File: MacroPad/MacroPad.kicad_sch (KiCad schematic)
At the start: 1 part

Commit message: RGB LED Circuit
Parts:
- added D? (x12): WS2812B, LED_SMD:LED_WS2812B_PLCC4_5.0x5.0mm_P3.2mm, symbol LED:WS2812B
- added R?: 470R, symbol Device:R
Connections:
- net GND: now reaches U?.14 (GND)
- net GND: now also D?.3 (VSS), D?.3 (VSS), D?.3 (VSS), D?.3 (VSS), D?.3 (VSS), D?.3 (VSS), D?.3 (VSS), D?.3 (VSS), D?.3 (VSS), D?.3 (VSS), D?.3 (VSS), D?.3 (VSS)
- net Vin: now reaches U?.19 (5V)
- net Vin: now also D?.1 (VDD), D?.1 (VDD), D?.1 (VDD), D?.1 (VDD), D?.1 (VDD), D?.1 (VDD), D?.1 (VDD), D?.1 (VDD), D?.1 (VDD), D?.1 (VDD), D?.1 (VDD), D?.1 (VDD)
- net DATA: now reaches U?.33 (GPIO21)
- net DATA: now also R?.1
- new net: D?.2 (DOUT), D?.4 (DIN) (x11)
- new net: D?.4 (DIN), R?.2
- no-connect marks 0 -> 1
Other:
- note added: "RGB LED Circuit"

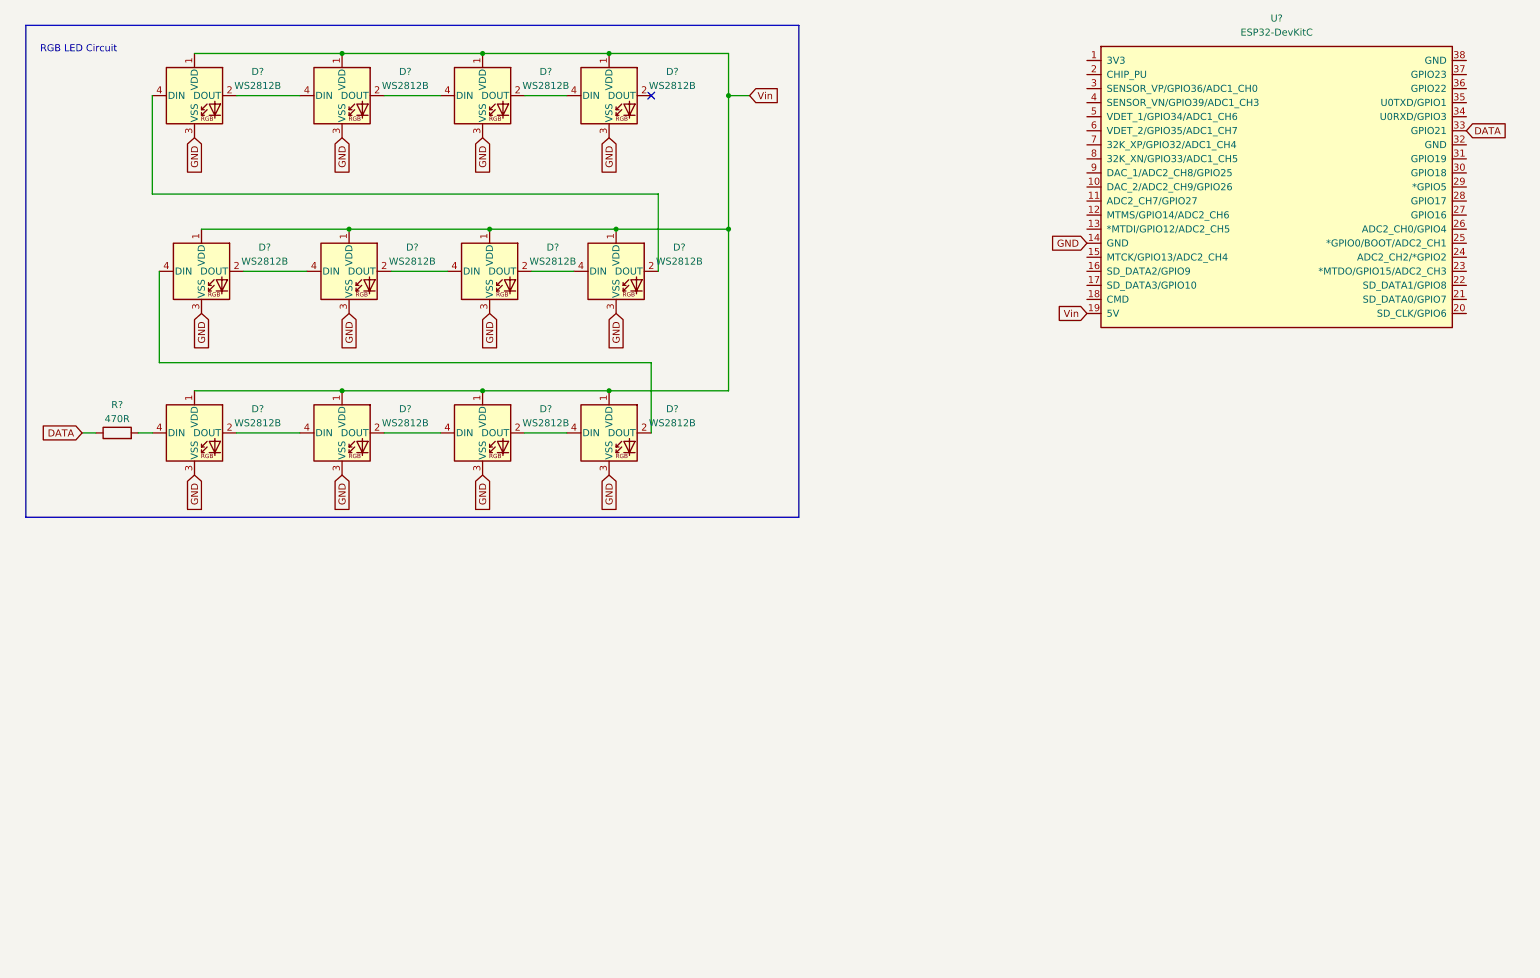
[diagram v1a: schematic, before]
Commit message: Switches Added to schematic
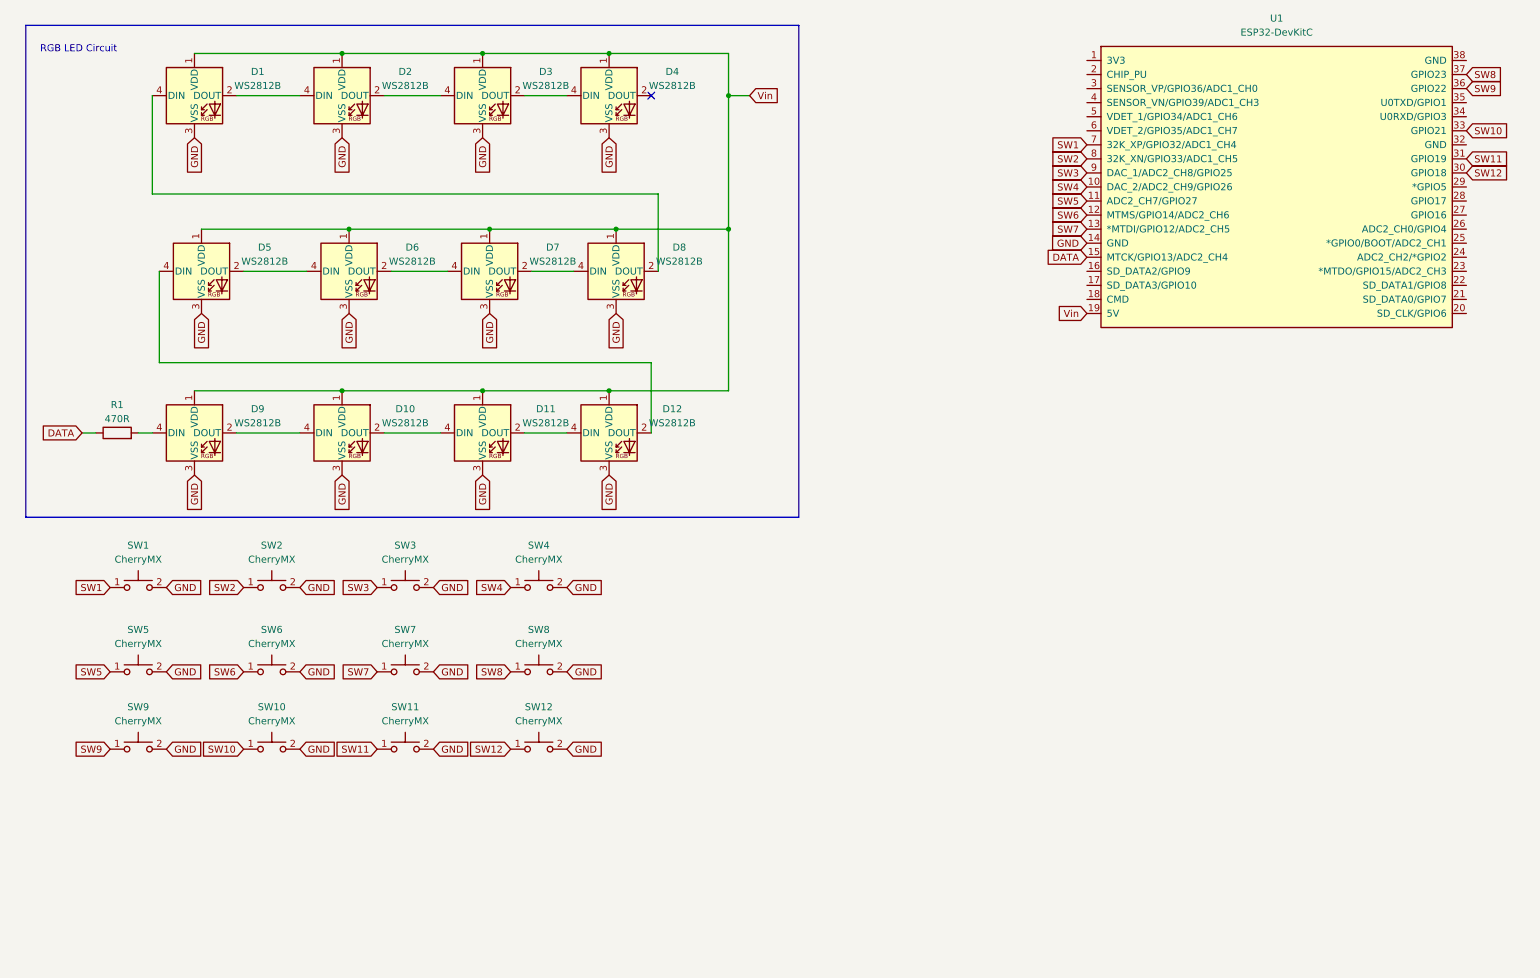
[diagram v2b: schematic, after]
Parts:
- added SW1, SW10, SW11, SW12, SW2, SW3, SW4, SW5, SW6, SW7, SW8, SW9: CherryMX, symbol CherryMX:CherryMX
- gave numbers to parts that had none: 14
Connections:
- net DATA: now also U1.15 (MTCK/GPIO13/ADC2_CH4); no longer U1.33 (GPIO21)
- net GND: now also SW1.2, SW10.2, SW11.2, SW12.2, SW2.2, SW3.2, SW4.2, SW5.2, SW6.2, SW7.2, SW8.2, SW9.2
- net SW4: now reaches U1.10 (DAC_2/ADC2_CH9/GPIO26)
- net SW4: now also SW4.1
- net SW5: now reaches U1.11 (ADC2_CH7/GPIO27)
- net SW5: now also SW5.1
- net SW6: now reaches U1.12 (MTMS/GPIO14/ADC2_CH6)
- net SW6: now also SW6.1
- net SW7: now reaches U1.13 (*MTDI/GPIO12/ADC2_CH5)
- net SW7: now also SW7.1
- net SW12: now reaches U1.30 (GPIO18)
- net SW12: now also SW12.1
- net SW11: now reaches U1.31 (GPIO19)
- net SW11: now also SW11.1
- net SW9: now reaches U1.36 (GPIO22)
- net SW9: now also SW9.1
- net SW8: now reaches U1.37 (GPIO23)
- net SW8: now also SW8.1
- net SW1: now reaches U1.7 (32K_XP/GPIO32/ADC1_CH4)
- net SW1: now also SW1.1
- net SW2: now reaches U1.8 (32K_XN/GPIO33/ADC1_CH5)
- net SW2: now also SW2.1
- net SW3: now reaches U1.9 (DAC_1/ADC2_CH8/GPIO25)
- net SW3: now also SW3.1
- new net SW10: SW10.1, U1.33 (GPIO21)

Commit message: forgot smth
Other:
- note added: "Keyboard Switches"
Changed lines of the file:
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@@
+    (stroke (width 0) (type default) (color 0 0 0 0))
+  )
+  (polyline (pts (xy 153.67 111.76) (xy 153.67 154.94))
     (stroke (width 0) (type default) (color 0 0 0 0))
   )
@@
   )
   (wire (pts (xy 140.97 25.4) (xy 140.97 33.02))
+    (stroke (width 0) (type default) (color 0 0 0 0))
+  )
+  (polyline (pts (xy 13.97 154.94) (xy 13.97 109.22))
     (stroke (width 0) (type default) (color 0 0 0 0))
   )
@@
     (stroke (width 0) (type default) (color 0 0 0 0))
   )
+  (polyline (pts (xy 153.67 154.94) (xy 13.97 154.94))
+    (stroke (width 0) (type default) (color 0 0 0 0))
+  )
+  (text "Keyboard Switches\n" (at 127 116.84 0)
+    (effects (font (size 1.27 1.27)) (justify left bottom))
+  )
   (text "RGB LED Circuit" (at 30.48 25.4 180)

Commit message: added capacitor to Keyboard Circuit to ground from Vin
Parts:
- added C?: 10u, symbol Device:C
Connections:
- net GND: now also C?.2
- net Vin: now also C?.1
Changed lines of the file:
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@@
   (junction (at 71.12 25.4) (diameter 0) (color 0 0 0 0)
+  )
+  (junction (at 140.97 48.26) (diameter 0) (color 0 0 0 0)
   )
   (junction (at 97.79 57.15) (diameter 0) (color 0 0 0 0)
@@
     (stroke (width 0) (type default) (color 0 0 0 0))
   )
+  (wire (pts (xy 140.97 48.26) (xy 140.97 57.15))
+    (stroke (width 0) (type default) (color 0 0 0 0))
+  )
   (wire (pts (xy 38.1 81.28) (xy 38.1 64.77))
     (stroke (width 0) (type default) (color 0 0 0 0))
@@
     (stroke (width 0) (type default) (color 0 0 0 0))
   )
-  (wire (pts (xy 140.97 33.02) (xy 140.97 57.15))
+  (wire (pts (xy 140.97 33.02) (xy 140.97 48.26))
     (stroke (width 0) (type default) (color 0 0 0 0))
   )
@@
     (stroke (width 0) (type default) (color 0 0 0 0))
   )
+  (wire (pts (xy 140.97 48.26) (xy 146.05 48.26))
+    (stroke (width 0) (type default) (color 0 0 0 0))
+  )
   (polyline (pts (xy 153.67 109.22) (xy 13.97 109.22))
     (stroke (width 0) (type default) (color 0 0 0 0))
@@
   )
   (wire (pts (xy 34.29 93.98) (xy 36.83 93.98))
+    (stroke (width 0) (type default) (color 0 0 0 0))
+  )
+  (wire (pts (xy 146.05 48.26) (xy 146.05 50.8))
     (stroke (width 0) (type default) (color 0 0 0 0))
   )
@@
     )
   )
+  (global_label "GND" (shape input) (at 146.05 58.42 270) (fields_autoplaced)
+    (effects (font (size 1.27 1.27)) (justify right))
+    (property "Intersheet References" "${INTERSHEET_REFS}" (id 0) (at 145.9706 64.7036 90)
+      (effects (font (size 1.27 1.27)) (justify right) hide)
+    )
+  )
   (global_label "GND" (shape input) (at 96.52 101.6 270) (fields_autoplaced)
     (effects (font (size 1.27 1.27)) (justify right))
@@
       (effects (font (size 1.27 1.27)) (justify right) hide)
     )
+  )
+  (symbol (lib_id "Device:C") (at 146.05 54.61 0) (unit 1)
+    (in_bom yes) (on_board yes) (fields_autoplaced)
+    (property "Reference" "C?" (id 0) (at 149.86 53.3399 0)
+      (effects (font (size 1.27 1.27)) (justify left))
+    )
+    (property "Value" "10u" (id 1) (at 149.86 55.8799 0)
+      (effects (font (size 1.27 1.27)) (justify left))
+    )
+    (property "Footprint" "" (id 2) (at 147.0152 58.42 0)
+      (effects (font (size 1.27 1.27)) hide)
+    )
+    (property "Datasheet" "~" (id 3) (at 146.05 54.61 0)
+      (effects (font (size 1.27 1.27)) hide)
+    )
+    (pin "1")
+    (pin "2")
   )
   (symbol (lib_id "CherryMX:CherryMX") (at 82.55 121.92 0) (unit 1)
@@
   )
   (symbol_instances
+    (path "/0e4e0ff0-9fdd-47a1-9807-a63ef4a30a92"
+      (reference "C?") (unit 1) (value "10u") (footprint "")
+    )
     (path "/a6694369-d7a9-41d0-a88e-8a3c16982564"
       (reference "D1") (unit 1) (value "WS2812B") (footprint "LED_SMD:LED_WS2812B_PLCC4_5.0x5.0mm_P3.2mm")

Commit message: initial PCB
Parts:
- C1: renamed from C?; footprint (none) -> Capacitor_SMD:C_1206_3216Metric_Pad1.33x1.80mm_HandSolder
- R1: footprint (none) -> Resistor_SMD:R_1206_3216Metric_Pad1.30x1.75mm_HandSolder
- SW1, SW10, SW11, SW12, SW2, SW3, SW4, SW5, SW6, SW7, SW8, SW9: footprint (none) -> Switch_Keyboard_Cherry_MX:SW_Cherry_MX_Plate_1.00u
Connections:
- no-connect marks 1 -> 24

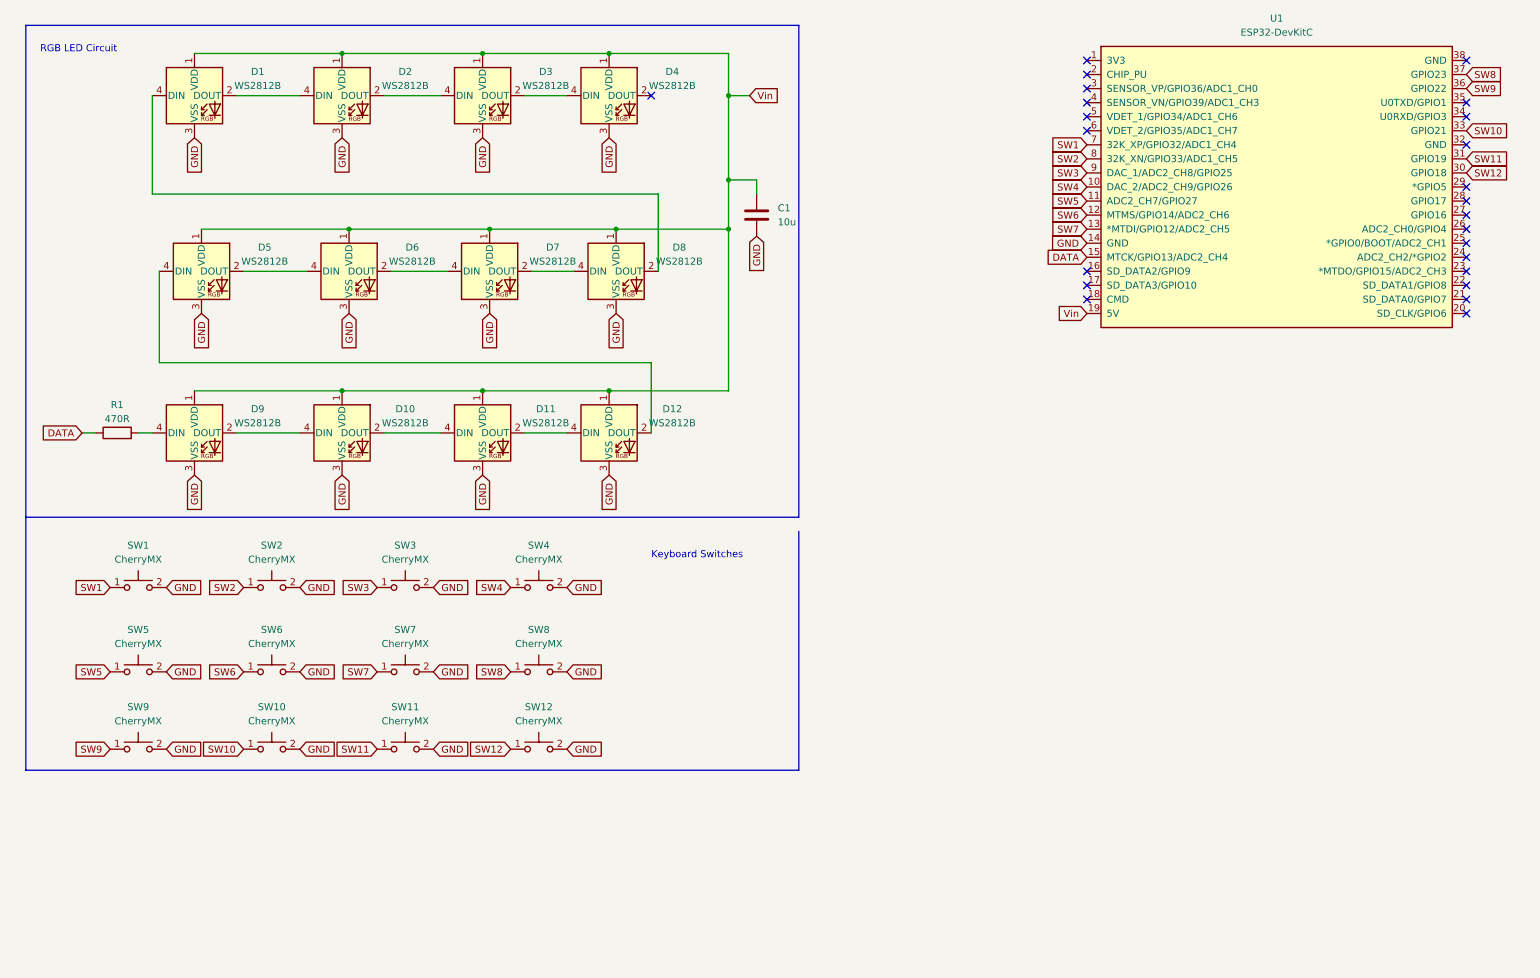
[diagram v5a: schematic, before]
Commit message: Started PCB todo: ground and vin connections
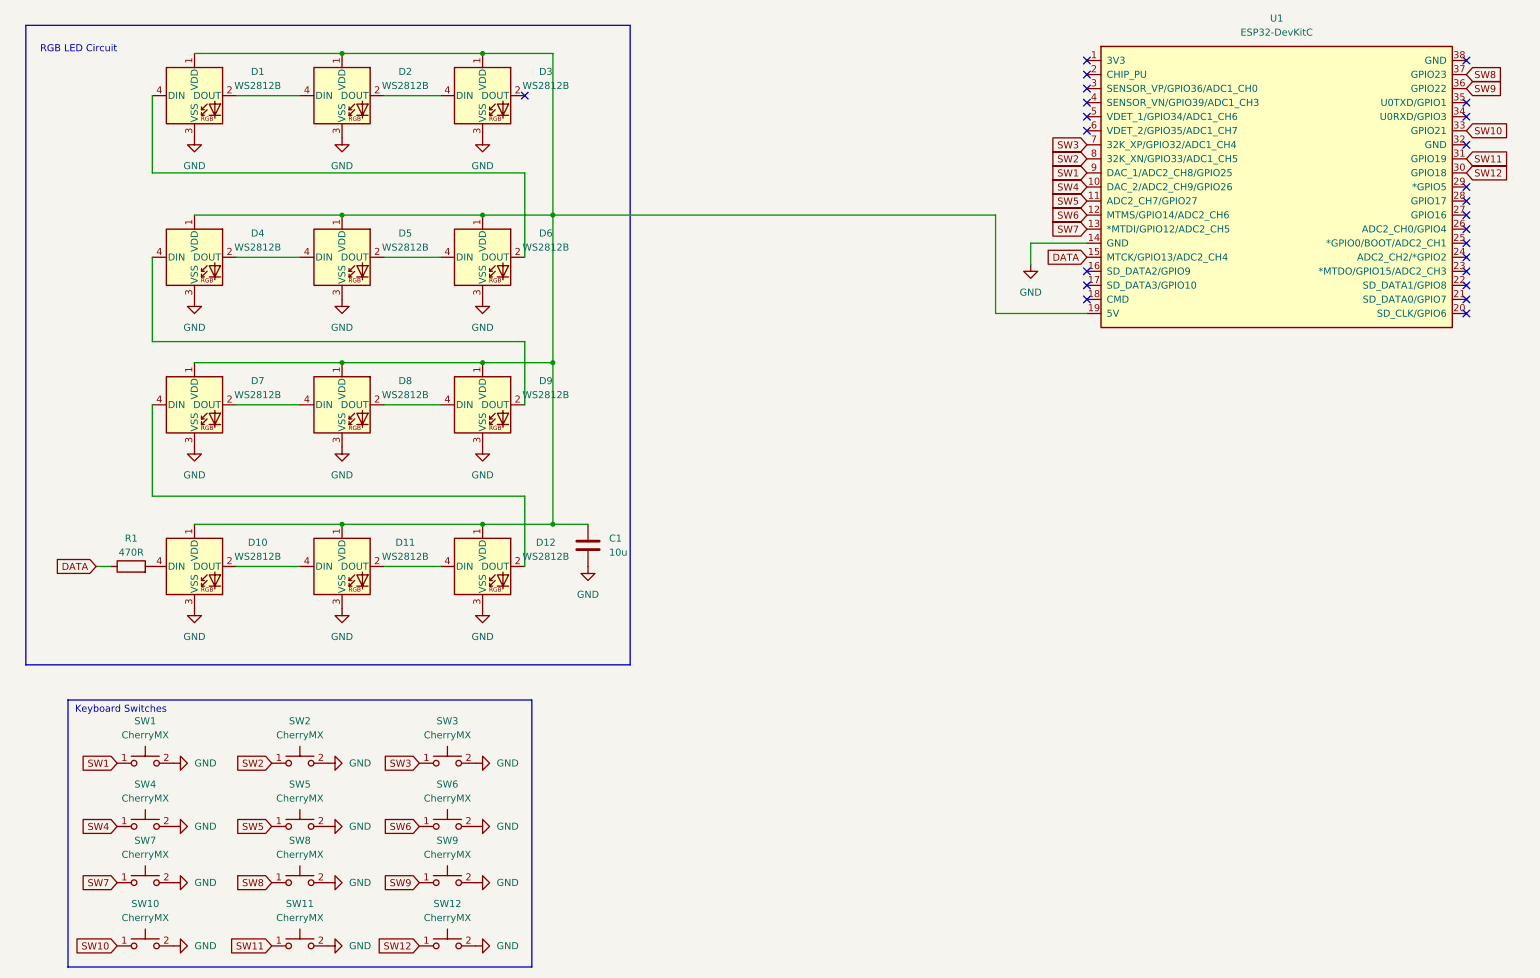
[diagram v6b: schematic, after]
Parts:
- removed D1, D10, D11, D12, D2, D3, D4, D5, D6, D7, D8, D9: WS2812B, LED_SMD:LED_WS2812B_PLCC4_5.0x5.0mm_P3.2mm, symbol LED:WS2812B
- added D1, D10, D11, D12, D2, D3, D4, D5, D6, D7, D8, D9: WS2812B, LED_SMD:LED_WS2812B_PLCC4_5.0x5.0mm_P3.2mm, symbol leds:WS2812B
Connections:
- net GND: now also D1.3 (VSS), D10.3 (VSS), D11.3 (VSS), D12.3 (VSS), D2.3 (VSS), D3.3 (VSS), D4.3 (VSS), D5.3 (VSS), D6.3 (VSS), D7.3 (VSS), D8.3 (VSS), D9.3 (VSS)
- net SW1: now also U1.9 (DAC_1/ADC2_CH8/GPIO25); no longer U1.7 (32K_XP/GPIO32/ADC1_CH4)
- net SW3: now also U1.7 (32K_XP/GPIO32/ADC1_CH4); no longer U1.9 (DAC_1/ADC2_CH8/GPIO25)
- net at R1.2: now also D10.4 (DIN)
- net Vin: no longer names the net of C1.1, U1.19 (5V)
- net Vin: now also D1.1 (VDD), D10.1 (VDD), D11.1 (VDD), D12.1 (VDD), D2.1 (VDD), D3.1 (VDD), D4.1 (VDD), D5.1 (VDD), D6.1 (VDD), D7.1 (VDD), D8.1 (VDD), D9.1 (VDD)
- new net: D10.2 (DOUT), D11.4 (DIN)
- new net: D4.2 (DOUT), D5.4 (DIN)
- new net: D4.4 (DIN), D9.2 (DOUT)
- new net: D12.2 (DOUT), D7.4 (DIN)
- new net: D11.2 (DOUT), D12.4 (DIN)
- new net: D7.2 (DOUT), D8.4 (DIN)
- new net: D8.2 (DOUT), D9.4 (DIN)
- new net: D1.2 (DOUT), D2.4 (DIN)
- new net: D1.4 (DIN), D6.2 (DOUT)
- new net: D2.2 (DOUT), D3.4 (DIN)
- new net: D5.2 (DOUT), D6.4 (DIN)
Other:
- moved on the sheet: R1, SW1, SW10, SW11, SW12, SW2, SW3, SW4, SW5, SW6, SW7, SW8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
